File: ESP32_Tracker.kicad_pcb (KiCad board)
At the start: 4 copper layers, 60 x 75 mm, 75 parts, among them J2 Conn_01x02_Socket, J3 Conn_01x03, J4 MSD-4-A, J5 Conn_01x07_Socket, J6 USB_C_Receptacle_USB2.0_16P, SW1 SW_Push, SW2 SW_Push, SW3 SW_Push, SW4 SW_Push, SW5 SW_Push, U1 USBLC6-2SC6, U2 ESP32-S3-MINI-1, U3 MP2667, U4 XC6220B331MR-G, U5 LIS2MDL, U6 SAM-M10Q

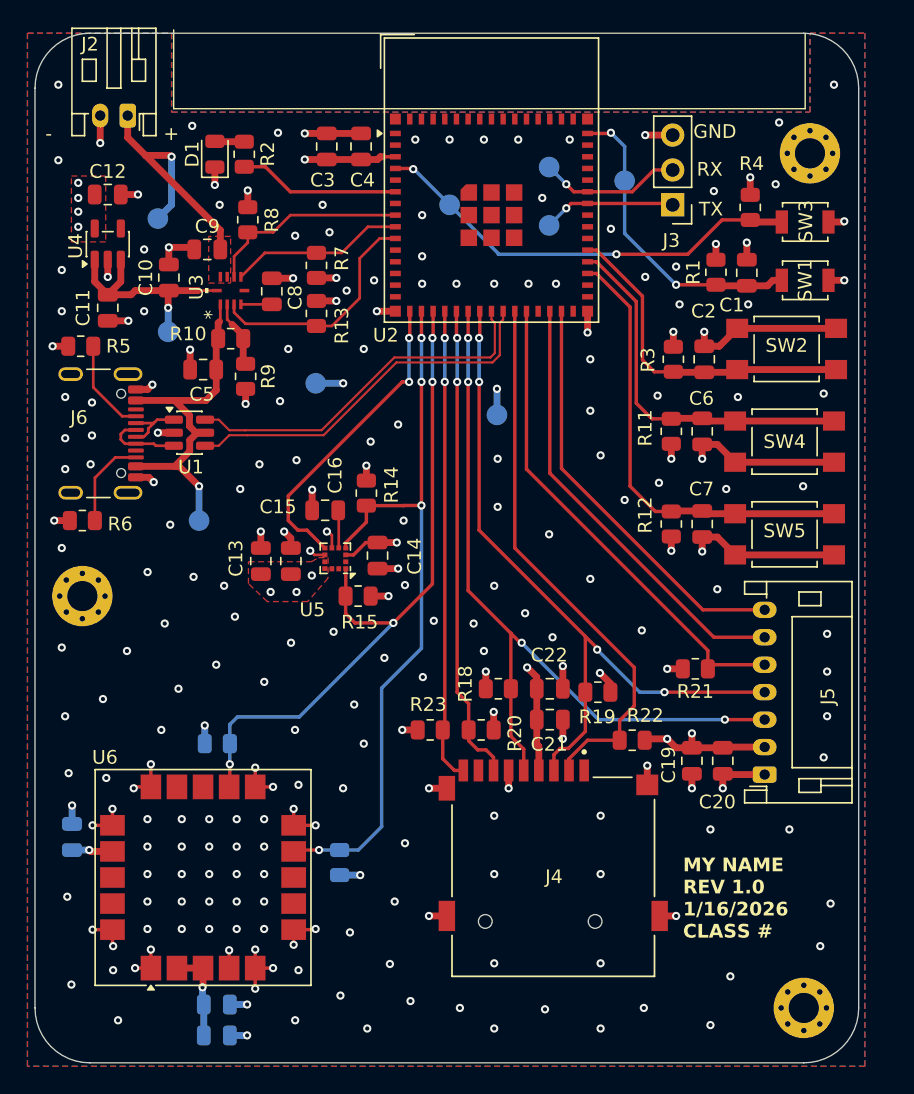
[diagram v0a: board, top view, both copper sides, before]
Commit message: changed to 8 pin connector
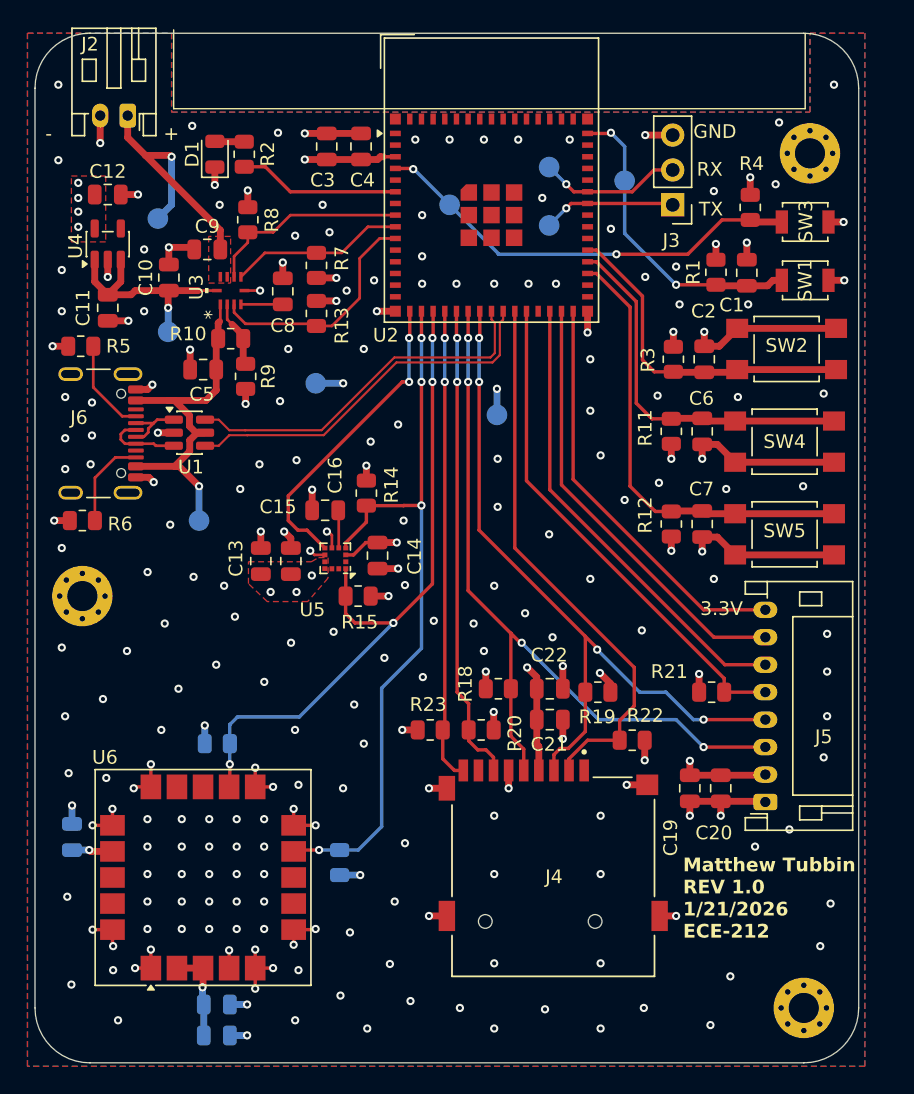
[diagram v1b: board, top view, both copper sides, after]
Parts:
- J5: value Conn_01x07_Socket -> Conn_01x08_Socket; footprint Connector_JST:JST_PH_S7B-PH-K_1x07_P2.00mm_Horizontal -> Connector_JST:JST_PH_S8B-PH-K_1x08_P2.00mm_Horizontal
- moved R21 2.07 mm to (163.3, 110.0)
- moved C19 2.01 mm to (161.8, 117.0)
- moved C20 2.01 mm to (164.0, 117.0)
- moved J5 2.00 mm to (167.2, 118.0)
- moved C8 0.80 mm to (132.1, 80.8)
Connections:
- U2 pad 30: unconnected-(U2-IO48-Pad30) -> /MCU/PWR/OLED_DET
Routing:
- net /MCU/PWR/OLED_DET: track 0.00 -> 30.2 mm
- net GND: track 120.0 -> 123.2 mm, vias 220 -> 221
- net +3.3V: track 62.4 -> 60.6 mm
- net /MCU/PWR/OLED_RST: track 30.5 -> 32.1 mm
- net /MCU/PWR/OLED_DC: track 32.4 -> 34.0 mm
- net /MCU/PWR/OLED_CS: track 35.8 -> 36.7 mm
- net /MCU/PWR/OLED/SD_MOSI: track 52.9 -> 53.7 mm
- net /MCU/PWR/OLED/SD_SCK: track 56.2 -> 57.1 mm
- net Net-(U3-VDD): track 2.25 -> 3.05 mm
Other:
- board text added: "Matthew Tubbin REV 1.0 1/21/2026 ECE-212"
- board text removed: "MY NAME REV 1.0 1/16/2026 CLASS #"

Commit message: REV 1.0 Ordered
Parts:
- renumbered C6 to C10, C23 to C19, C3 to C2, C19 to C20, C20 to C21, C21 to C22, C22 to C23, C4 to C3, C5 to C4, C2 to C5, C7 to C6, C8 to C7, C9 to C8, C10 to C9, J6 to J1, J3 to J2, J2 to J3, J5 to J4, J4 to J5, R12 to R11, R13 to R12, R11 to R13, R4 to R3, R5 to R4, R6 to R5, R7 to R6, R8 to R7, R9 to R8, R3 to R9, SW3 to SW2, SW2 to SW3, SW5 to SW4, SW4 to SW5, TP5 to TP2, TP4 to TP3, TP9 to TP4, TP2 to TP5, TP3 to TP6, TP6 to TP7, TP7 to TP8, TP8 to TP9
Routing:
- net GND: track 123.2 -> 125.7 mm, vias 221 -> 223
